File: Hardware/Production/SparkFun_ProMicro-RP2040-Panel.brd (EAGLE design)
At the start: 132.1 x 140 mm, 1611 parts, among them J1 Qwiic, J12 USB Female Type C Connector, J13 Qwiic, J16 USB Female Type C Connector, J17 Qwiic, J2 Qwiic, J20 USB Female Type C Connector, J21 Qwiic, J24 USB Female Type C Connector, J25 Qwiic, J28 USB Female Type C Connector, J29 Qwiic, J32 USB Female Type C Connector, J33 Qwiic, J36 USB Female Type C Connector, J37 Qwiic, J40 USB Female Type C Connector, J41 Qwiic, J44 USB Female Type C Connector, J45 Qwiic, J48 USB Female Type C Connector, J49 Qwiic, J5 USB Female Type C Connector, J52 USB Female Type C Connector, J53 Qwiic, J56 USB Female Type C Connector, J57 Qwiic, J60 USB Female Type C Connector, J8 USB Female Type C Connector, J9 Qwiic, U1 3.3V, U10 RP2040, U11 W25QXX128MBIT, U12 WS2812-2020, U13 3.3V, U14 RP2040, U15 W25QXX128MBIT, U16 WS2812-2020, U17 3.3V, U18 RP2040, U19 W25QXX128MBIT, U2 RP2040, U20 WS2812-2020, U21 3.3V, U22 RP2040, U23 W25QXX128MBIT, U24 WS2812-2020, U25 3.3V, U26 RP2040, U27 W25QXX128MBIT, U28 WS2812-2020, U29 3.3V, U3 WS2812-2020, U30 RP2040, U31 W25QXX128MBIT, U32 WS2812-2020, U33 3.3V, U34 RP2040, U35 W25QXX128MBIT, U36 WS2812-2020, U37 3.3V, U38 RP2040, U39 W25QXX128MBIT, U4 W25QXX128MBIT, U40 WS2812-2020, U41 3.3V, U42 RP2040, U43 W25QXX128MBIT, U44 WS2812-2020, U45 3.3V, U46 RP2040, U47 W25QXX128MBIT, U48 WS2812-2020, U49 3.3V, U5 3.3V, U50 RP2040, U51 W25QXX128MBIT, U52 WS2812-2020, U53 3.3V, U54 RP2040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

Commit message: New panel
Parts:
- added C271, C289, C307, C325, C343, C361, C379, C397, C415: 1.0uF, SparkFun-Capacitors:0402-TIGHT
- added C272, C273, C290, C291, C308, C309, C326, C327, C344, C345, C362, C363, C380, C381, C398, C399, C416, C417: 10uF, SparkFun-Capacitors:0402-TIGHT
- added C274, C275, C292, C293, C310, C311, C328, C329, C346, C347, C364, C365, C382, C383, C400, C401, C418, C419: 15pF, SparkFun-Capacitors:0402-TIGHT
- added C276, C277, C278, C279, C280, C281, C282, C283, C287, C294, C295, C296, C297, C298, C299, C300, C301, C305, C312, C313, C314, C315, C316, C317, C318, C319, C323, C330, C331, C332, C333, C334, C335, C336, C337, C341, C348, C349, C350, C351, C352, C353, C354, C355, C359, C366, C367, C368, C369, C370, C371, C372, C373, C377, C384, C385, C386, C387, C388, C389, C390, C391, C395, C402, C403, C404, C405, C406, C407, C408, C409, C413, C420, C421, C422, C423, C424, C425, C426, C427, C431: 0.1uF, SparkFun-Capacitors:0402-TIGHT
- added C284, C285, C286, C288, C302, C303, C304, C306, C320, C321, C322, C324, C338, C339, C340, C342, C356, C357, C358, C360, C374, C375, C376, C378, C392, C393, C394, C396, C410, C411, C412, C414, C428, C429, C430, C432: 2.2uF, SparkFun-Capacitors:0402-TIGHT
- added D16, D17, D18, D19, D20, D21, D22, D23, D24: 3A/10V/280mV, SparkFun-DiscreteSemi:SOD-323
- added F16, F17, F18, F19, F20, F21, F22, F23, F24: 6V 0.5A, SparkFun-Fuses:0805
- added J61, J65, J69, J73, J77, J81, J85, J89, J93: Qwiic, SparkFun-Connectors:JST04_1MM_RA
- added J62, J63, J66, J67, J70, J71, J74, J75, J78, J79, J82, J83, J86, J87, J90, J91, J94, J95: (no value), Castellated:1X12_CASTELLATED
- added J64, J68, J72, J76, J80, J84, J88, J92, J96: USB Female Type C Connector, SparkFun-Connectors:USB-C-16P_4LAYER-PADS
- added JP46, JP47, JP49, JP50, JP52, JP53, JP55, JP56, JP58, JP59, JP61, JP62, JP64, JP65, JP67, JP68, JP70, JP71: FIDUCIAL1X2, SparkFun-Aesthetics:FIDUCIAL-1X2
- added JP48, JP51, JP54, JP57, JP60, JP63, JP66, JP69, JP72: USB_SOLDER_PADS, SparkFun-Connectors:USB-SOLDER-PADS
- added LED16, LED17, LED18, LED19, LED20, LED21, LED22, LED23, LED24: RED, SparkFun-LED:LED-0603
- added LOGO46, LOGO49, LOGO52, LOGO55, LOGO58, LOGO61, LOGO64, LOGO67, LOGO70: SFE_LOGO_NAME_FLAME.1_INCH, SparkFun-Aesthetics:SFE_LOGO_NAME_FLAME_.1
- added LOGO47, LOGO50, LOGO53, LOGO56, LOGO59, LOGO62, LOGO65, LOGO68, LOGO71: QWIIC_LOGO_6MM, SparkFun-Aesthetics:QWIIC_6MM
- added LOGO48, LOGO51, LOGO54, LOGO57, LOGO60, LOGO63, LOGO66, LOGO69, LOGO72: SFE_LOGO_FLAME.1_INCH, SparkFun-Aesthetics:SFE_LOGO_FLAME_.1
- added R181, R187, R191, R193, R199, R203, R205, R211, R215, R217, R223, R227, R229, R235, R239, R241, R247, R251, R253, R259, R263, R265, R271, R275, R277, R283, R287: 1k, SparkFun-Resistors:0402-TIGHT
- added R182, R192, R194, R204, R206, R216, R218, R228, R230, R240, R242, R252, R254, R264, R266, R276, R278, R288: 10k, SparkFun-Resistors:0402-TIGHT
- added R183, R184, R195, R196, R207, R208, R219, R220, R231, R232, R243, R244, R255, R256, R267, R268, R279, R280: 5.1k, SparkFun-Resistors:0402-TIGHT
- added R185, R186, R197, R198, R209, R210, R221, R222, R233, R234, R245, R246, R257, R258, R269, R270, R281, R282: 2.2k, SparkFun-Resistors:0402-TIGHT
- added R188, R189, R200, R201, R212, R213, R224, R225, R236, R237, R248, R249, R260, R261, R272, R273, R284, R285: 27, SparkFun-Resistors:0402-TIGHT
- added R190, R202, R214, R226, R238, R250, R262, R274, R286: 200, SparkFun-Resistors:0402-TIGHT
- added S31, S33, S35, S37, S39, S41, S43, S45, S47: Reset, SparkFun-Switches:TACTILE_SWITCH_SMD_4.6X2.8MM
- added S32, S34, S36, S38, S40, S42, S44, S46, S48: Boot, SparkFun-Switches:TACTILE_SWITCH_SMD_4.6X2.8MM
- added TP46, TP47, TP48, TP49, TP50, TP51, TP52, TP53, TP54, TP55, TP56, TP57, TP58, TP59, TP60, TP61, TP62, TP63, TP64, TP65, TP66, TP67, TP68, TP69, TP70, TP71, TP72: (no value), SparkFun-Connectors:PAD.03X.05
- added U$1000, U$1030, U$1054, U$1084, U$1108, U$1138, U$1162, U$1192, U$1216, U$1246, U$1270, U$814, U$838, U$868, U$892, U$922, U$946, U$976: (no value), output:A21
- added U$1001, U$1031, U$1055, U$1085, U$1109, U$1139, U$1163, U$1193, U$1217, U$1247, U$1271, U$815, U$839, U$869, U$893, U$923, U$947, U$977: (no value), output:A32
- added U$1002, U$1045, U$1056, U$1099, U$1110, U$1153, U$1164, U$1207, U$1218, U$1261, U$1272, U$829, U$840, U$883, U$894, U$937, U$948, U$991: (no value), output:TX0
- added U$1003, U$1044, U$1057, U$1098, U$1111, U$1152, U$1165, U$1206, U$1219, U$1260, U$1273, U$828, U$841, U$882, U$895, U$936, U$949, U$990: (no value), output:RX1
- added U$1004, U$1017, U$1043, U$1058, U$1071, U$1097, U$1112, U$1125, U$1151, U$1166, U$1179, U$1205, U$1220, U$1233, U$1259, U$1274, U$1287, U$827, U$842, U$855, U$881, U$896, U$909, U$935, U$950, U$963, U$989: (no value), output:GND2
- added U$1005, U$1035, U$1059, U$1089, U$1113, U$1143, U$1167, U$1197, U$1221, U$1251, U$1275, U$819, U$843, U$873, U$897, U$927, U$951, U$981: (no value), output:20
- added U$1006, U$1036, U$1060, U$1090, U$1114, U$1144, U$1168, U$1198, U$1222, U$1252, U$1276, U$820, U$844, U$874, U$898, U$928, U$952, U$982: (no value), output:31
- added U$1007, U$1037, U$1061, U$1091, U$1115, U$1145, U$1169, U$1199, U$1223, U$1253, U$1277, U$821, U$845, U$875, U$899, U$929, U$953, U$983: (no value), output:42
- added U$1008, U$1038, U$1062, U$1092, U$1116, U$1146, U$1170, U$1200, U$1224, U$1254, U$1278, U$822, U$846, U$876, U$900, U$930, U$954, U$984: (no value), output:53
- added U$1009, U$1039, U$1063, U$1093, U$1117, U$1147, U$1171, U$1201, U$1225, U$1255, U$1279, U$823, U$847, U$877, U$901, U$931, U$955, U$985: (no value), output:64
- added U$1010, U$1064, U$1118, U$1172, U$1226, U$1280, U$848, U$902, U$956: (no value), output:D#1
- added U$1011, U$1065, U$1119, U$1173, U$1227, U$1281, U$849, U$903, U$957: (no value), output:D#2
- added U$1012, U$1066, U$1120, U$1174, U$1228, U$1282, U$850, U$904, U$958: (no value), output:G0
- added U$1013, U$1067, U$1121, U$1175, U$1229, U$1283, U$851, U$905, U$959: (no value), output:V3
- added U$1014, U$1068, U$1122, U$1176, U$1230, U$1284, U$852, U$906, U$960: (no value), output:210
- added U$1015, U$1069, U$1123, U$1177, U$1231, U$1285, U$853, U$907, U$961: (no value), output:#RST#0
- added U$1016, U$1070, U$1124, U$1178, U$1232, U$1286, U$854, U$908, U$962: (no value), output:3V3_0
- added U$1018, U$1072, U$1126, U$1180, U$1234, U$1288, U$856, U$910, U$964: (no value), output:RAW0
- added U$1019, U$1073, U$1127, U$1181, U$1235, U$1289, U$857, U$911, U$965: (no value), output:B0
- added U$1020, U$1074, U$1128, U$1182, U$1236, U$1290, U$858, U$912, U$966: (no value), output:R0
- added U$1021, U$1075, U$1129, U$1183, U$1237, U$1291, U$859, U$913, U$967: (no value), output:#0
- added U$1022, U$1076, U$1130, U$1184, U$1238, U$1292, U$860, U$914, U$968: (no value), output:PRO_MICRO0
- added U$1023, U$1077, U$1131, U$1185, U$1239, U$1293, U$861, U$915, U$969: (no value), output:RP20401
- added U$1024, U$1078, U$1132, U$1186, U$1240, U$1294, U$862, U$916, U$970: (no value), output:C0
- added U$1025, U$1079, U$1133, U$1187, U$1241, U$1295, U$863, U$917, U$971: (no value), output:D1
- added U$1026, U$1080, U$1134, U$1188, U$1242, U$1296, U$864, U$918, U$972: (no value), output:DO0
- added U$1027, U$1081, U$1135, U$1189, U$1243, U$811, U$865, U$919, U$973: OSHW-LOGOMINI, SparkFun-Aesthetics:OSHW-LOGO-MINI
- added U$1028, U$1052, U$1082, U$1106, U$1136, U$1160, U$1190, U$1214, U$1244, U$1268, U$812, U$836, U$866, U$890, U$920, U$944, U$974, U$998: (no value), output:A00
- added U$1029, U$1053, U$1083, U$1107, U$1137, U$1161, U$1191, U$1215, U$1245, U$1269, U$813, U$837, U$867, U$891, U$921, U$945, U$975, U$999: (no value), output:A10
- added U$1032, U$1050, U$1086, U$1104, U$1140, U$1158, U$1194, U$1212, U$1248, U$1266, U$816, U$834, U$870, U$888, U$924, U$942, U$978, U$996: (no value), output:CI4
- added U$1033, U$1087, U$1141, U$1195, U$1249, U$817, U$871, U$925, U$979: (no value), output:CO5
- added U$1034, U$1051, U$1088, U$1105, U$1142, U$1159, U$1196, U$1213, U$1250, U$1267, U$818, U$835, U$872, U$889, U$926, U$943, U$980, U$997: (no value), output:SCK3
- added U$1040, U$1094, U$1148, U$1202, U$1256, U$824, U$878, U$932, U$986: (no value), output:#RST#1
- added U$1041, U$1095, U$1149, U$1203, U$1257, U$825, U$879, U$933, U$987: (no value), output:3V30
- added U$1042, U$1096, U$1150, U$1204, U$1258, U$826, U$880, U$934, U$988: (no value), output:PWR0
- added U$1046, U$1100, U$1154, U$1208, U$1262, U$830, U$884, U$938, U$992: (no value), output:GND_0
- added U$1047, U$1101, U$1155, U$1209, U$1263, U$831, U$885, U$939, U$993: (no value), output:70
- added U$1048, U$1102, U$1156, U$1210, U$1264, U$832, U$886, U$940, U$994: (no value), output:81
- added U$1049, U$1103, U$1157, U$1211, U$1265, U$833, U$887, U$941, U$995: (no value), output:92
- added U61, U65, U69, U73, U77, U81, U85, U89, U93: 3.3V, SparkFun-IC-Power:SOT23-5
- added U62, U66, U70, U74, U78, U82, U86, U90, U94: RP2040, RP2040:QFN-56
- added U63, U67, U71, U75, U79, U83, U87, U91, U95: W25QXX128MBIT, SparkFun-IC-Memory:WSON-8-6X5-SKINNY_CENTERPAD
- added U64, U68, U72, U76, U80, U84, U88, U92, U96: WS2812-2020, SparkFun-LED:WS2812-2020
- added Y16, Y17, Y18, Y19, Y20, Y21, Y22, Y23, Y24: 12MHz, SparkFun-Clocks:CRYSTAL-SMD-2X2.5MM
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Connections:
- new net !RESET!15: J63.3, J63.3B, R182.1, S31.3, S31.4, U62.26
- new net !RESET!16: J67.3, J67.3B, R194.1, S33.3, S33.4, U66.26
- new net !RESET!17: J71.3, J71.3B, R206.1, S35.3, S35.4, U70.26
- new net !RESET!18: J75.3, J75.3B, R218.1, S37.3, S37.4, U74.26
- new net !RESET!19: J79.3, J79.3B, R230.1, S39.3, S39.4, U78.26
- new net !RESET!20: J83.3, J83.3B, R242.1, S41.3, S41.4, U82.26
- new net !RESET!21: J87.3, J87.3B, R254.1, S43.3, S43.4, U86.26
- new net !RESET!22: J91.3, J91.3B, R266.1, S45.3, S45.4, U90.26
- new net !RESET!23: J95.3, J95.3B, R278.1, S47.3, S47.4, U94.26
- new net 0/TX15: J62.12, J62.12B, U62.2
- new net 0/TX16: J66.12, J66.12B, U66.2
- new net 0/TX17: J70.12, J70.12B, U70.2
- new net 0/TX18: J74.12, J74.12B, U74.2
- new net 0/TX19: J78.12, J78.12B, U78.2
- new net 0/TX20: J82.12, J82.12B, U82.2
- new net 0/TX21: J86.12, J86.12B, U86.2
- new net 0/TX22: J90.12, J90.12B, U90.2
- new net 0/TX23: J94.12, J94.12B, U94.2
- new net 1.1V15: C282.1, C283.1, C284.1, U62.23, U62.45, U62.50
- new net 1.1V16: C300.1, C301.1, C302.1, U66.23, U66.45, U66.50
- new net 1.1V17: C318.1, C319.1, C320.1, U70.23, U70.45, U70.50
- new net 1.1V18: C336.1, C337.1, C338.1, U74.23, U74.45, U74.50
- new net 1.1V19: C354.1, C355.1, C356.1, U78.23, U78.45, U78.50
- new net 1.1V20: C372.1, C373.1, C374.1, U82.23, U82.45, U82.50
- new net 1.1V21: C390.1, C391.1, C392.1, U86.23, U86.45, U86.50
- new net 1.1V22: C408.1, C409.1, C410.1, U90.23, U90.45, U90.50
- new net 1.1V23: C426.1, C427.1, C428.1, U94.23, U94.45, U94.50
- new net 1/RX15: J62.11, J62.11B, U62.3
- new net 1/RX16: J66.11, J66.11B, U66.3
- new net 1/RX17: J70.11, J70.11B, U70.3
- new net 1/RX18: J74.11, J74.11B, U74.3
- new net 1/RX19: J78.11, J78.11B, U78.3
- new net 1/RX20: J82.11, J82.11B, U82.3
- new net 1/RX21: J86.11, J86.11B, U86.3
- new net 1/RX22: J90.11, J90.11B, U90.3
- new net 1/RX23: J94.11, J94.11B, U94.3
- new net 100: J66.3, J66.3B, U66.9
- new net 101: J66.8, J66.8B, U66.4
- new net 102: J66.7, J66.7B, U66.5
- new net 103: J70.5, J70.5B, U70.7
- new net 104: J70.6, J70.6B, U70.6
- new net 105: J70.4, J70.4B, U70.8
- new net 106: J70.3, J70.3B, U70.9
- new net 107: J70.8, J70.8B, U70.4
- new net 108: J70.7, J70.7B, U70.5
- new net 109: J74.5, J74.5B, U74.7
- new net 110: J74.6, J74.6B, U74.6
- new net 111: J74.4, J74.4B, U74.8
- new net 112: J74.3, J74.3B, U74.9
- new net 113: J74.8, J74.8B, U74.4
- new net 114: J74.7, J74.7B, U74.5
- new net 115: J78.5, J78.5B, U78.7
- new net 116: J78.6, J78.6B, U78.6
- new net 117: J78.4, J78.4B, U78.8
- new net 118: J78.3, J78.3B, U78.9
- new net 119: J78.8, J78.8B, U78.4
- new net 120: J78.7, J78.7B, U78.5
- new net 121: J82.5, J82.5B, U82.7
- new net 122: J82.6, J82.6B, U82.6
- new net 123: J82.4, J82.4B, U82.8
- new net 124: J82.3, J82.3B, U82.9
- new net 125: J82.8, J82.8B, U82.4
- new net 126: J82.7, J82.7B, U82.5
- new net 127: J86.5, J86.5B, U86.7
- new net 128: J86.6, J86.6B, U86.6
- new net 129: J86.4, J86.4B, U86.8
- new net 130: J86.3, J86.3B, U86.9
- new net 131: J86.8, J86.8B, U86.4
- new net 132: J86.7, J86.7B, U86.5
- new net 133: J90.5, J90.5B, U90.7
- new net 134: J90.6, J90.6B, U90.6
- new net 135: J90.4, J90.4B, U90.8
- new net 136: J90.3, J90.3B, U90.9
- new net 137: J90.8, J90.8B, U90.4
- new net 138: J90.7, J90.7B, U90.5
- new net 139: J94.5, J94.5B, U94.7
- new net 140: J94.6, J94.6B, U94.6
- new net 141: J94.4, J94.4B, U94.8
- new net 142: J94.3, J94.3B, U94.9
- new net 143: J94.8, J94.8B, U94.4
- new net 144: J94.7, J94.7B, U94.5
- new net 16/SDA15: J61.3, R185.1, U62.27
- new net 16/SDA16: J65.3, R197.1, U66.27
- new net 16/SDA17: J69.3, R209.1, U70.27
- new net 16/SDA18: J73.3, R221.1, U74.27
- new net 16/SDA19: J77.3, R233.1, U78.27
- new net 16/SDA20: J81.3, R245.1, U82.27
- new net 16/SDA21: J85.3, R257.1, U86.27
- new net 16/SDA22: J89.3, R269.1, U90.27
- new net 16/SDA23: J93.3, R281.1, U94.27
- new net 17/SCL15: J61.4, R186.1, U62.28
- new net 17/SCL16: J65.4, R198.1, U66.28
- new net 17/SCL17: J69.4, R210.1, U70.28
- new net 17/SCL18: J73.4, R222.1, U74.28
- new net 17/SCL19: J77.4, R234.1, U78.28
- new net 17/SCL20: J81.4, R246.1, U82.28
- new net 17/SCL21: J85.4, R258.1, U86.28
- new net 17/SCL22: J89.4, R270.1, U90.28
- new net 17/SCL23: J93.4, R282.1, U94.28
- new net 20/SPI_CIPO15: J63.10, J63.10B, U62.31
- new net 20/SPI_CIPO16: J67.10, J67.10B, U66.31
- new net 20/SPI_CIPO17: J71.10, J71.10B, U70.31
- new net 20/SPI_CIPO18: J75.10, J75.10B, U74.31
- new net 20/SPI_CIPO19: J79.10, J79.10B, U78.31
- new net 20/SPI_CIPO20: J83.10, J83.10B, U82.31
- new net 20/SPI_CIPO21: J87.10, J87.10B, U86.31
- new net 20/SPI_CIPO22: J91.10, J91.10B, U90.31
- new net 20/SPI_CIPO23: J95.10, J95.10B, U94.31
- new net 21/SPI_!CS!15: J63.12, J63.12B, U62.32
- new net 21/SPI_!CS!16: J67.12, J67.12B, U66.32
- new net 21/SPI_!CS!17: J71.12, J71.12B, U70.32
- new net 21/SPI_!CS!18: J75.12, J75.12B, U74.32
- new net 21/SPI_!CS!19: J79.12, J79.12B, U78.32
- new net 21/SPI_!CS!20: J83.12, J83.12B, U82.32
- new net 21/SPI_!CS!21: J87.12, J87.12B, U86.32
- new net 21/SPI_!CS!22: J91.12, J91.12B, U90.32
- new net 21/SPI_!CS!23: J95.12, J95.12B, U94.32
- new net 22/SPI_SCK15: J63.9, J63.9B, U62.34
- new net 22/SPI_SCK16: J67.9, J67.9B, U66.34
- new net 22/SPI_SCK17: J71.9, J71.9B, U70.34
- new net 22/SPI_SCK18: J75.9, J75.9B, U74.34
- new net 22/SPI_SCK19: J79.9, J79.9B, U78.34
- new net 22/SPI_SCK20: J83.9, J83.9B, U82.34
- new net 22/SPI_SCK21: J87.9, J87.9B, U86.34
- new net 22/SPI_SCK22: J91.9, J91.9B, U90.34
- new net 22/SPI_SCK23: J95.9, J95.9B, U94.34
- new net 23/SPI_COPI15: J63.11, J63.11B, U62.35
- new net 23/SPI_COPI16: J67.11, J67.11B, U66.35
- new net 23/SPI_COPI17: J71.11, J71.11B, U70.35
- new net 23/SPI_COPI18: J75.11, J75.11B, U74.35
- new net 23/SPI_COPI19: J79.11, J79.11B, U78.35
- new net 23/SPI_COPI20: J83.11, J83.11B, U82.35
- new net 23/SPI_COPI21: J87.11, J87.11B, U86.35
- new net 23/SPI_COPI22: J91.11, J91.11B, U90.35
- new net 23/SPI_COPI23: J95.11, J95.11B, U94.35
- new net 25/WS2812-DI15: U62.37, U64.3
- new net 25/WS2812-DI16: U66.37, U68.3
- new net 25/WS2812-DI17: U70.37, U72.3
- new net 25/WS2812-DI18: U74.37, U76.3
- new net 25/WS2812-DI19: U78.37, U80.3
- new net 25/WS2812-DI20: U82.37, U84.3
- new net 25/WS2812-DI21: U86.37, U88.3
- new net 25/WS2812-DI22: U90.37, U92.3
- new net 25/WS2812-DI23: U94.37, U96.3
- new net 3.3V15: C273.2, C276.1, C277.1, C278.1, C279.1, C280.1, C281.1, C285.1, C287.1, C288.1, J61.2, J63.4, J63.4B, R181.2, R182.2, R185.2, R186.2, R190.2, R192.2, U61.5, U62.1, U62.10, U62.22, U62.33, U62.42, U62.44, U62.48, U62.49, U63.8
- new net 3.3V16: C291.2, C294.1, C295.1, C296.1, C297.1, C298.1, C299.1, C303.1, C305.1, C306.1, J65.2, J67.4, J67.4B, R193.2, R194.2, R197.2, R198.2, R202.2, R204.2, U65.5, U66.1, U66.10, U66.22, U66.33, U66.42, U66.44, U66.48, U66.49, U67.8
- new net 3.3V17: C309.2, C312.1, C313.1, C314.1, C315.1, C316.1, C317.1, C321.1, C323.1, C324.1, J69.2, J71.4, J71.4B, R205.2, R206.2, R209.2, R210.2, R214.2, R216.2, U69.5, U70.1, U70.10, U70.22, U70.33, U70.42, U70.44, U70.48, U70.49, U71.8
- new net 3.3V18: C327.2, C330.1, C331.1, C332.1, C333.1, C334.1, C335.1, C339.1, C341.1, C342.1, J73.2, J75.4, J75.4B, R217.2, R218.2, R221.2, R222.2, R226.2, R228.2, U73.5, U74.1, U74.10, U74.22, U74.33, U74.42, U74.44, U74.48, U74.49, U75.8
- new net 3.3V19: C345.2, C348.1, C349.1, C350.1, C351.1, C352.1, C353.1, C357.1, C359.1, C360.1, J77.2, J79.4, J79.4B, R229.2, R230.2, R233.2, R234.2, R238.2, R240.2, U77.5, U78.1, U78.10, U78.22, U78.33, U78.42, U78.44, U78.48, U78.49, U79.8
- new net 3.3V20: C363.2, C366.1, C367.1, C368.1, C369.1, C370.1, C371.1, C375.1, C377.1, C378.1, J81.2, J83.4, J83.4B, R241.2, R242.2, R245.2, R246.2, R250.2, R252.2, U81.5, U82.1, U82.10, U82.22, U82.33, U82.42, U82.44, U82.48, U82.49, U83.8
- new net 3.3V21: C381.2, C384.1, C385.1, C386.1, C387.1, C388.1, C389.1, C393.1, C395.1, C396.1, J85.2, J87.4, J87.4B, R253.2, R254.2, R257.2, R258.2, R262.2, R264.2, U85.5, U86.1, U86.10, U86.22, U86.33, U86.42, U86.44, U86.48, U86.49, U87.8
- new net 3.3V22: C399.2, C402.1, C403.1, C404.1, C405.1, C406.1, C407.1, C411.1, C413.1, C414.1, J89.2, J91.4, J91.4B, R265.2, R266.2, R269.2, R270.2, R274.2, R276.2, U89.5, U90.1, U90.10, U90.22, U90.33, U90.42, U90.44, U90.48, U90.49, U91.8
- new net 3.3V23: C417.2, C420.1, C421.1, C422.1, C423.1, C424.1, C425.1, C429.1, C431.1, C432.1, J93.2, J95.4, J95.4B, R277.2, R278.2, R281.2, R282.2, R286.2, R288.2, U93.5, U94.1, U94.10, U94.22, U94.33, U94.42, U94.44, U94.48, U94.49, U95.8
- new net 8/TX16: J62.2, J62.2B, U62.11
- new net 8/TX17: J66.2, J66.2B, U66.11
- new net 8/TX18: J70.2, J70.2B, U70.11
- new net 8/TX19: J74.2, J74.2B, U74.11
- new net 8/TX20: J78.2, J78.2B, U78.11
- new net 8/TX21: J82.2, J82.2B, U82.11
- new net 8/TX22: J86.2, J86.2B, U86.11
- new net 8/TX23: J90.2, J90.2B, U90.11
- new net 8/TX24: J94.2, J94.2B, U94.11
- new net 9/RX16: J62.1, J62.1B, U62.12
- new net 9/RX17: J66.1, J66.1B, U66.12
- new net 9/RX18: J70.1, J70.1B, U70.12
- new net 9/RX19: J74.1, J74.1B, U74.12
- new net 9/RX20: J78.1, J78.1B, U78.12
- new net 9/RX21: J82.1, J82.1B, U82.12
- new net 9/RX22: J86.1, J86.1B, U86.12
- new net 9/RX23: J90.1, J90.1B, U90.12
- new net 9/RX24: J94.1, J94.1B, U94.12
- new net 91: J62.5, J62.5B, U62.7
- new net 92: J62.6, J62.6B, U62.6
- new net 93: J62.4, J62.4B, U62.8
- new net 94: J62.3, J62.3B, U62.9
- new net 95: J62.8, J62.8B, U62.4
- new net 96: J62.7, J62.7B, U62.5
- new net 97: J66.5, J66.5B, U66.7
- new net 98: J66.6, J66.6B, U66.6
- new net 99: J66.4, J66.4B, U66.8
- new net A60: J63.5, J63.5B, U62.41
- new net A61: J63.6, J63.6B, U62.40
- new net A62: J63.7, J63.7B, U62.39
- new net A63: J63.8, J63.8B, U62.38
- new net A64: J67.5, J67.5B, U66.41
- new net A65: J67.6, J67.6B, U66.40
- new net A66: J67.7, J67.7B, U66.39
- new net A67: J67.8, J67.8B, U66.38
- new net A68: J71.5, J71.5B, U70.41
- new net A69: J71.6, J71.6B, U70.40
- new net A70: J71.7, J71.7B, U70.39
- new net A71: J71.8, J71.8B, U70.38
- new net A72: J75.5, J75.5B, U74.41
- new net A73: J75.6, J75.6B, U74.40
- new net A74: J75.7, J75.7B, U74.39
- new net A75: J75.8, J75.8B, U74.38
- new net A76: J79.5, J79.5B, U78.41
- new net A77: J79.6, J79.6B, U78.40
- new net A78: J79.7, J79.7B, U78.39
- new net A79: J79.8, J79.8B, U78.38
- new net A80: J83.5, J83.5B, U82.41
- new net A81: J83.6, J83.6B, U82.40
- new net A82: J83.7, J83.7B, U82.39
- new net A83: J83.8, J83.8B, U82.38
- new net A84: J87.5, J87.5B, U86.41
- new net A85: J87.6, J87.6B, U86.40
- new net A86: J87.7, J87.7B, U86.39
- new net A87: J87.8, J87.8B, U86.38
- new net A88: J91.5, J91.5B, U90.41
- new net A89: J91.6, J91.6B, U90.40
- new net A90: J91.7, J91.7B, U90.39
- new net A91: J91.8, J91.8B, U90.38
- new net A92: J95.5, J95.5B, U94.41
- new net A93: J95.6, J95.6B, U94.40
- new net A94: J95.7, J95.7B, U94.39
- new net A95: J95.8, J95.8B, U94.38
- new net ADC_VDD15: C286.1, R190.1, U62.43
- new net ADC_VDD16: C304.1, R202.1, U66.43
- new net ADC_VDD17: C322.1, R214.1, U70.43
- new net ADC_VDD18: C340.1, R226.1, U74.43
- new net ADC_VDD19: C358.1, R238.1, U78.43
- new net ADC_VDD20: C376.1, R250.1, U82.43
- new net ADC_VDD21: C394.1, R262.1, U86.43
- new net ADC_VDD22: C412.1, R274.1, U90.43
- new net ADC_VDD23: C430.1, R286.1, U94.43
- new net BOOT15: R191.2, S32.3, S32.4
- new net BOOT16: R203.2, S34.3, S34.4
- new net BOOT17: R215.2, S36.3, S36.4
- new net BOOT18: R227.2, S38.3, S38.4
- new net BOOT19: R239.2, S40.3, S40.4
- new net BOOT20: R251.2, S42.3, S42.4
- new net BOOT21: R263.2, S44.3, S44.4
- new net BOOT22: R275.2, S46.3, S46.4
- new net BOOT23: R287.2, S48.3, S48.4
- new net GND15: C271.1, C272.1, C273.1, C274.1, C275.1, C276.2, C277.2, C278.2, C279.2, C280.2, C281.2, C282.2, C283.2, C284.2, C285.2, C286.2, C287.2, C288.2, J61.1, J62.10, J62.10B, J62.9, J62.9B, J63.2, J63.2B, J64.GND, J64.GND2, JP48.GND, LED16.C, R183.1, R184.1, S31.1, S31.2, S32.1, S32.2, U61.2, U62.19, U62.EPAD, U63.4, U64.2
- new net GND16: C289.1, C290.1, C291.1, C292.1, C293.1, C294.2, C295.2, C296.2, C297.2, C298.2, C299.2, C300.2, C301.2, C302.2, C303.2, C304.2, C305.2, C306.2, J65.1, J66.10, J66.10B, J66.9, J66.9B, J67.2, J67.2B, J68.GND, J68.GND2, JP51.GND, LED17.C, R195.1, R196.1, S33.1, S33.2, S34.1, S34.2, U65.2, U66.19, U66.EPAD, U67.4, U68.2
- new net GND17: C307.1, C308.1, C309.1, C310.1, C311.1, C312.2, C313.2, C314.2, C315.2, C316.2, C317.2, C318.2, C319.2, C320.2, C321.2, C322.2, C323.2, C324.2, J69.1, J70.10, J70.10B, J70.9, J70.9B, J71.2, J71.2B, J72.GND, J72.GND2, JP54.GND, LED18.C, R207.1, R208.1, S35.1, S35.2, S36.1, S36.2, U69.2, U70.19, U70.EPAD, U71.4, U72.2
- new net GND18: C325.1, C326.1, C327.1, C328.1, C329.1, C330.2, C331.2, C332.2, C333.2, C334.2, C335.2, C336.2, C337.2, C338.2, C339.2, C340.2, C341.2, C342.2, J73.1, J74.10, J74.10B, J74.9, J74.9B, J75.2, J75.2B, J76.GND, J76.GND2, JP57.GND, LED19.C, R219.1, R220.1, S37.1, S37.2, S38.1, S38.2, U73.2, U74.19, U74.EPAD, U75.4, U76.2
- new net GND19: C343.1, C344.1, C345.1, C346.1, C347.1, C348.2, C349.2, C350.2, C351.2, C352.2, C353.2, C354.2, C355.2, C356.2, C357.2, C358.2, C359.2, C360.2, J77.1, J78.10, J78.10B, J78.9, J78.9B, J79.2, J79.2B, J80.GND, J80.GND2, JP60.GND, LED20.C, R231.1, R232.1, S39.1, S39.2, S40.1, S40.2, U77.2, U78.19, U78.EPAD, U79.4, U80.2
- new net GND20: C361.1, C362.1, C363.1, C364.1, C365.1, C366.2, C367.2, C368.2, C369.2, C370.2, C371.2, C372.2, C373.2, C374.2, C375.2, C376.2, C377.2, C378.2, J81.1, J82.10, J82.10B, J82.9, J82.9B, J83.2, J83.2B, J84.GND, J84.GND2, JP63.GND, LED21.C, R243.1, R244.1, S41.1, S41.2, S42.1, S42.2, U81.2, U82.19, U82.EPAD, U83.4, U84.2
- new net GND21: C379.1, C380.1, C381.1, C382.1, C383.1, C384.2, C385.2, C386.2, C387.2, C388.2, C389.2, C390.2, C391.2, C392.2, C393.2, C394.2, C395.2, C396.2, J85.1, J86.10, J86.10B, J86.9, J86.9B, J87.2, J87.2B, J88.GND, J88.GND2, JP66.GND, LED22.C, R255.1, R256.1, S43.1, S43.2, S44.1, S44.2, U85.2, U86.19, U86.EPAD, U87.4, U88.2
- new net GND22: C397.1, C398.1, C399.1, C400.1, C401.1, C402.2, C403.2, C404.2, C405.2, C406.2, C407.2, C408.2, C409.2, C410.2, C411.2, C412.2, C413.2, C414.2, J89.1, J90.10, J90.10B, J90.9, J90.9B, J91.2, J91.2B, J92.GND, J92.GND2, JP69.GND, LED23.C, R267.1, R268.1, S45.1, S45.2, S46.1, S46.2, U89.2, U90.19, U90.EPAD, U91.4, U92.2
- new net GND23: C415.1, C416.1, C417.1, C418.1, C419.1, C420.2, C421.2, C422.2, C423.2, C424.2, C425.2, C426.2, C427.2, C428.2, C429.2, C430.2, C431.2, C432.2, J93.1, J94.10, J94.10B, J94.9, J94.9B, J95.2, J95.2B, J96.GND, J96.GND2, JP72.GND, LED24.C, R279.1, R280.1, S47.1, S47.2, S48.1, S48.2, U93.2, U94.19, U94.EPAD, U95.4, U96.2
- new net N$61: LED16.A, R181.1
- new net N$62: J64.A5, R184.2
- new net N$63: J64.B5, R183.2
- new net N$64: TP48.P$1, U64.1
- new net N$65: LED17.A, R193.1
- new net N$66: J68.A5, R196.2
- new net N$67: J68.B5, R195.2
- new net N$68: TP51.P$1, U68.1
- new net N$69: LED18.A, R205.1
- new net N$70: J72.A5, R208.2
- new net N$71: J72.B5, R207.2
- new net N$72: TP54.P$1, U72.1
- new net N$73: LED19.A, R217.1
- new net N$74: J76.A5, R220.2
- new net N$75: J76.B5, R219.2
- new net N$76: TP57.P$1, U76.1
- new net N$77: LED20.A, R229.1
- new net N$78: J80.A5, R232.2
- new net N$79: J80.B5, R231.2
- new net N$80: TP60.P$1, U80.1
- new net N$81: LED21.A, R241.1
- new net N$82: J84.A5, R244.2
- new net N$83: J84.B5, R243.2
- new net N$84: TP63.P$1, U84.1
- new net N$85: LED22.A, R253.1
- new net N$86: J88.A5, R256.2
- new net N$87: J88.B5, R255.2
- new net N$88: TP66.P$1, U88.1
- new net N$89: LED23.A, R265.1
- new net N$90: J92.A5, R268.2
- new net N$91: J92.B5, R267.2
- new net N$92: TP69.P$1, U92.1
- new net N$93: LED24.A, R277.1
- new net N$94: J96.A5, R280.2
- new net N$95: J96.B5, R279.2
- new net N$96: TP72.P$1, U96.1
- new net QSPI-60: U62.53, U63.5
- new net QSPI-61: U62.51, U63.7
- new net QSPI-62: U62.55, U63.2
- new net QSPI-63: U62.54, U63.3
- new net QSPI-64: U66.53, U67.5
- new net QSPI-65: U66.51, U67.7
- new net QSPI-66: U66.55, U67.2
- new net QSPI-67: U66.54, U67.3
- new net QSPI-68: U70.53, U71.5
- new net QSPI-69: U70.51, U71.7
- new net QSPI-70: U70.55, U71.2
- new net QSPI-71: U70.54, U71.3
- new net QSPI-72: U74.53, U75.5
- new net QSPI-73: U74.51, U75.7
- new net QSPI-74: U74.55, U75.2
- new net QSPI-75: U74.54, U75.3
- new net QSPI-76: U78.53, U79.5
- new net QSPI-77: U78.51, U79.7
- new net QSPI-78: U78.55, U79.2
- new net QSPI-79: U78.54, U79.3
- new net QSPI-80: U82.53, U83.5
- new net QSPI-81: U82.51, U83.7
- new net QSPI-82: U82.55, U83.2
- new net QSPI-83: U82.54, U83.3
- new net QSPI-84: U86.53, U87.5
- new net QSPI-85: U86.51, U87.7
- new net QSPI-86: U86.55, U87.2
- new net QSPI-87: U86.54, U87.3
- new net QSPI-88: U90.53, U91.5
- new net QSPI-89: U90.51, U91.7
- new net QSPI-90: U90.55, U91.2
- new net QSPI-91: U90.54, U91.3
- new net QSPI-92: U94.53, U95.5
- new net QSPI-93: U94.51, U95.7
- new net QSPI-94: U94.55, U95.2
- new net QSPI-95: U94.54, U95.3
- new net QSPI-CLK15: U62.52, U63.6
- new net QSPI-CLK16: U66.52, U67.6
- new net QSPI-CLK17: U70.52, U71.6
- new net QSPI-CLK18: U74.52, U75.6
- new net QSPI-CLK19: U78.52, U79.6
- new net QSPI-CLK20: U82.52, U83.6
- new net QSPI-CLK21: U86.52, U87.6
- new net QSPI-CLK22: U90.52, U91.6
- new net QSPI-CLK23: U94.52, U95.6
- new net QSPI-CS15: R191.1, R192.1, U62.56, U63.1
- new net QSPI-CS16: R203.1, R204.1, U66.56, U67.1
- new net QSPI-CS17: R215.1, R216.1, U70.56, U71.1
- new net QSPI-CS18: R227.1, R228.1, U74.56, U75.1
- new net QSPI-CS19: R239.1, R240.1, U78.56, U79.1
- new net QSPI-CS20: R251.1, R252.1, U82.56, U83.1
- new net QSPI-CS21: R263.1, R264.1, U86.56, U87.1
- new net QSPI-CS22: R275.1, R276.1, U90.56, U91.1
- new net QSPI-CS23: R287.1, R288.1, U94.56, U95.1
- new net RAW15: C272.2, D16.C, J63.1, J63.1B, U61.1, U61.3, U64.4
- new net RAW16: C290.2, D17.C, J67.1, J67.1B, U65.1, U65.3, U68.4
- new net RAW17: C308.2, D18.C, J71.1, J71.1B, U69.1, U69.3, U72.4
- new net RAW18: C326.2, D19.C, J75.1, J75.1B, U73.1, U73.3, U76.4
- new net RAW19: C344.2, D20.C, J79.1, J79.1B, U77.1, U77.3, U80.4
- new net RAW20: C362.2, D21.C, J83.1, J83.1B, U81.1, U81.3, U84.4
- new net RAW21: C380.2, D22.C, J87.1, J87.1B, U85.1, U85.3, U88.4
- new net RAW22: C398.2, D23.C, J91.1, J91.1B, U89.1, U89.3, U92.4
- new net RAW23: C416.2, D24.C, J95.1, J95.1B, U93.1, U93.3, U96.4
- new net RP_D+15: J64.A6, J64.B6, JP48.D+, R189.1
- new net RP_D+16: J68.A6, J68.B6, JP51.D+, R201.1
- new net RP_D+17: J72.A6, J72.B6, JP54.D+, R213.1
- new net RP_D+18: J76.A6, J76.B6, JP57.D+, R225.1
- new net RP_D+19: J80.A6, J80.B6, JP60.D+, R237.1
- new net RP_D+20: J84.A6, J84.B6, JP63.D+, R249.1
- new net RP_D+21: J88.A6, J88.B6, JP66.D+, R261.1
- new net RP_D+22: J92.A6, J92.B6, JP69.D+, R273.1
- new net RP_D+23: J96.A6, J96.B6, JP72.D+, R285.1
- new net RP_D-15: J64.A7, J64.B7, JP48.D-, R188.1
- new net RP_D-16: J68.A7, J68.B7, JP51.D-, R200.1
- new net RP_D-17: J72.A7, J72.B7, JP54.D-, R212.1
- new net RP_D-18: J76.A7, J76.B7, JP57.D-, R224.1
- new net RP_D-19: J80.A7, J80.B7, JP60.D-, R236.1
- new net RP_D-20: J84.A7, J84.B7, JP63.D-, R248.1
- new net RP_D-21: J88.A7, J88.B7, JP66.D-, R260.1
- new net RP_D-22: J92.A7, J92.B7, JP69.D-, R272.1
- new net RP_D-23: J96.A7, J96.B7, JP72.D-, R284.1
- new net RP_D1+15: R189.2, U62.47
- new net RP_D1+16: R201.2, U66.47
- new net RP_D1+17: R213.2, U70.47
- new net RP_D1+18: R225.2, U74.47
- new net RP_D1+19: R237.2, U78.47
- new net RP_D1+20: R249.2, U82.47
- new net RP_D1+21: R261.2, U86.47
- new net RP_D1+22: R273.2, U90.47
- new net RP_D1+23: R285.2, U94.47
- new net RP_D1-15: R188.2, U62.46
- new net RP_D1-16: R200.2, U66.46
- new net RP_D1-17: R212.2, U70.46
- new net RP_D1-18: R224.2, U74.46
- new net RP_D1-19: R236.2, U78.46
- new net RP_D1-20: R248.2, U82.46
- new net RP_D1-21: R260.2, U86.46
- new net RP_D1-22: R272.2, U90.46
- new net RP_D1-23: R284.2, U94.46
- new net SWDCK15: TP46.P$1, U62.24
- new net SWDCK16: TP49.P$1, U66.24
- new net SWDCK17: TP52.P$1, U70.24
- new net SWDCK18: TP55.P$1, U74.24
- new net SWDCK19: TP58.P$1, U78.24
- new net SWDCK20: TP61.P$1, U82.24
- new net SWDCK21: TP64.P$1, U86.24
- new net SWDCK22: TP67.P$1, U90.24
- new net SWDCK23: TP70.P$1, U94.24
- new net SWDIO15: TP47.P$1, U62.25
- new net SWDIO16: TP50.P$1, U66.25
- new net SWDIO17: TP53.P$1, U70.25
- new net SWDIO18: TP56.P$1, U74.25
- new net SWDIO19: TP59.P$1, U78.25
- new net SWDIO20: TP62.P$1, U82.25
- new net SWDIO21: TP65.P$1, U86.25
- new net SWDIO22: TP68.P$1, U90.25
- new net SWDIO23: TP71.P$1, U94.25
- new net USB_RAW15: D16.A, F16.2
- new net USB_RAW16: D17.A, F17.2
- new net USB_RAW17: D18.A, F18.2
- new net USB_RAW18: D19.A, F19.2
- new net USB_RAW19: D20.A, F20.2
- new net USB_RAW20: D21.A, F21.2
- new net USB_RAW21: D22.A, F22.2
- new net USB_RAW22: D23.A, F23.2
- new net USB_RAW23: D24.A, F24.2
- new net V_USB15: C271.2, F16.1, J64.VBUS1, J64.VBUS2, JP48.VBUS
- new net V_USB16: C289.2, F17.1, J68.VBUS1, J68.VBUS2, JP51.VBUS
- new net V_USB17: C307.2, F18.1, J72.VBUS1, J72.VBUS2, JP54.VBUS
- new net V_USB18: C325.2, F19.1, J76.VBUS1, J76.VBUS2, JP57.VBUS
- new net V_USB19: C343.2, F20.1, J80.VBUS1, J80.VBUS2, JP60.VBUS
- new net V_USB20: C361.2, F21.1, J84.VBUS1, J84.VBUS2, JP63.VBUS
- new net V_USB21: C379.2, F22.1, J88.VBUS1, J88.VBUS2, JP66.VBUS
- new net V_USB22: C397.2, F23.1, J92.VBUS1, J92.VBUS2, JP69.VBUS
- new net V_USB23: C415.2, F24.1, J96.VBUS1, J96.VBUS2, JP72.VBUS
- new net X16: C275.2, U62.20, Y16.P3
- new net X17: C293.2, U66.20, Y17.P3
- new net X18: C311.2, U70.20, Y18.P3
- new net X19: C329.2, U74.20, Y19.P3
- new net X1A15: R187.2, U62.21
- new net X1A16: R199.2, U66.21
- new net X1A17: R211.2, U70.21
- new net X1A18: R223.2, U74.21
- new net X1A19: R235.2, U78.21
- new net X1A20: R247.2, U82.21
- new net X1A21: R259.2, U86.21
- new net X1A22: R271.2, U90.21
- new net X1A23: R283.2, U94.21
- new net X1B15: C274.2, R187.1, Y16.P1
- new net X1B16: C292.2, R199.1, Y17.P1
- new net X1B17: C310.2, R211.1, Y18.P1
- new net X1B18: C328.2, R223.1, Y19.P1
- new net X1B19: C346.2, R235.1, Y20.P1
- new net X1B20: C364.2, R247.1, Y21.P1
- new net X1B21: C382.2, R259.1, Y22.P1
- new net X1B22: C400.2, R271.1, Y23.P1
- new net X1B23: C418.2, R283.1, Y24.P1
- new net X20: C347.2, U78.20, Y20.P3
- new net X21: C365.2, U82.20, Y21.P3
- new net X22: C383.2, U86.20, Y22.P3
- new net X23: C401.2, U90.20, Y23.P3
- new net X24: C419.2, U94.20, Y24.P3
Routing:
- net 3.3V20: track 0.00 -> 43.5 mm, vias 0 -> 10
- net 3.3V22: track 0.00 -> 43.5 mm, vias 0 -> 10
- net 3.3V21: track 0.00 -> 43.5 mm, vias 0 -> 10
- net 3.3V19: track 0.00 -> 43.5 mm, vias 0 -> 10
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- added copper zone on layer 15, net 3.3V15
- added copper zone on layer 15, net 3.3V16
- added copper zone on layer 15, net 3.3V17
- added copper zone on layer 15, net 3.3V18
- added copper zone on layer 15, net 3.3V19
- added copper zone on layer 15, net 3.3V20
- added copper zone on layer 15, net 3.3V21
- added copper zone on layer 15, net 3.3V22
- added copper zone on layer 15, net 3.3V23
- added copper zone on layer 1, net GND15
- added copper zone on layer 16, net GND15
- added copper zone on layer 2, net GND15
- added copper zone on layer 1, net GND16
- added copper zone on layer 16, net GND16
- added copper zone on layer 2, net GND16
- added copper zone on layer 1, net GND17
- added copper zone on layer 16, net GND17
- added copper zone on layer 2, net GND17
- added copper zone on layer 1, net GND18
- added copper zone on layer 16, net GND18
- added copper zone on layer 2, net GND18
- added copper zone on layer 1, net GND19
- added copper zone on layer 16, net GND19
- added copper zone on layer 2, net GND19
- added copper zone on layer 1, net GND20
- added copper zone on layer 16, net GND20
- added copper zone on layer 2, net GND20
- added copper zone on layer 1, net GND21
- added copper zone on layer 16, net GND21
- added copper zone on layer 2, net GND21
- added copper zone on layer 1, net GND22
- added copper zone on layer 16, net GND22
- added copper zone on layer 2, net GND22
- added copper zone on layer 1, net GND23
- added copper zone on layer 16, net GND23
- added copper zone on layer 2, net GND23
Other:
- board size 132.1 x 140 mm -> 212.1 x 134.6 mm
- board text added: "v-score"
- board text added: "v12"
- board text removed: "v11"

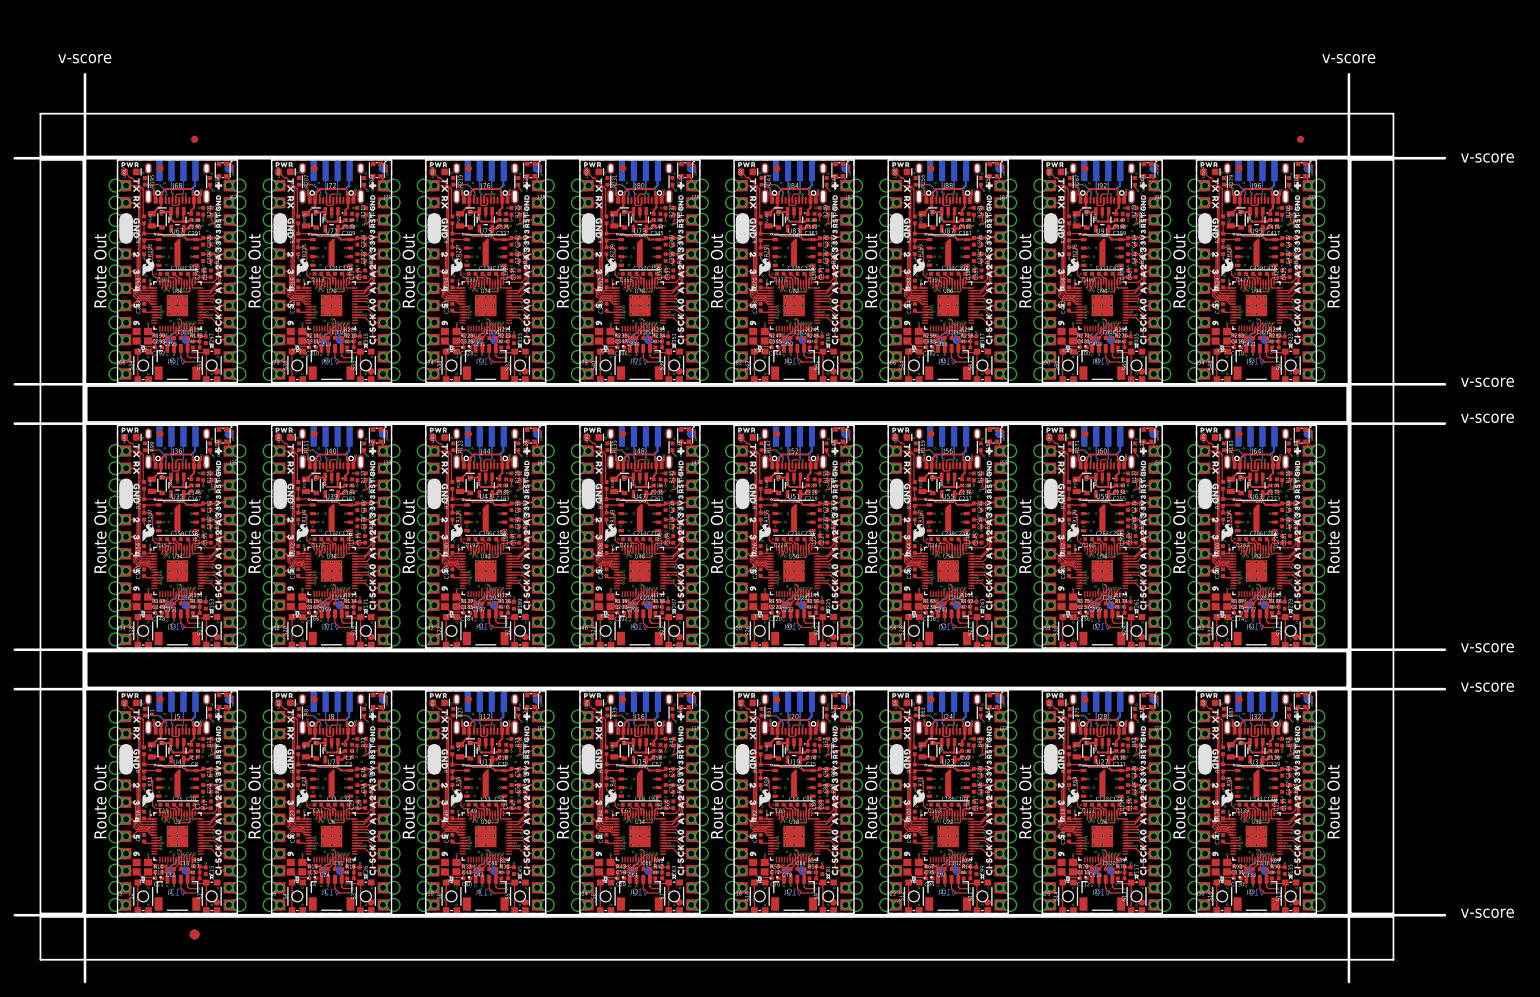
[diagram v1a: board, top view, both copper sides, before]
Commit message: Increase isolation in layers 2/15. Increase to v13.
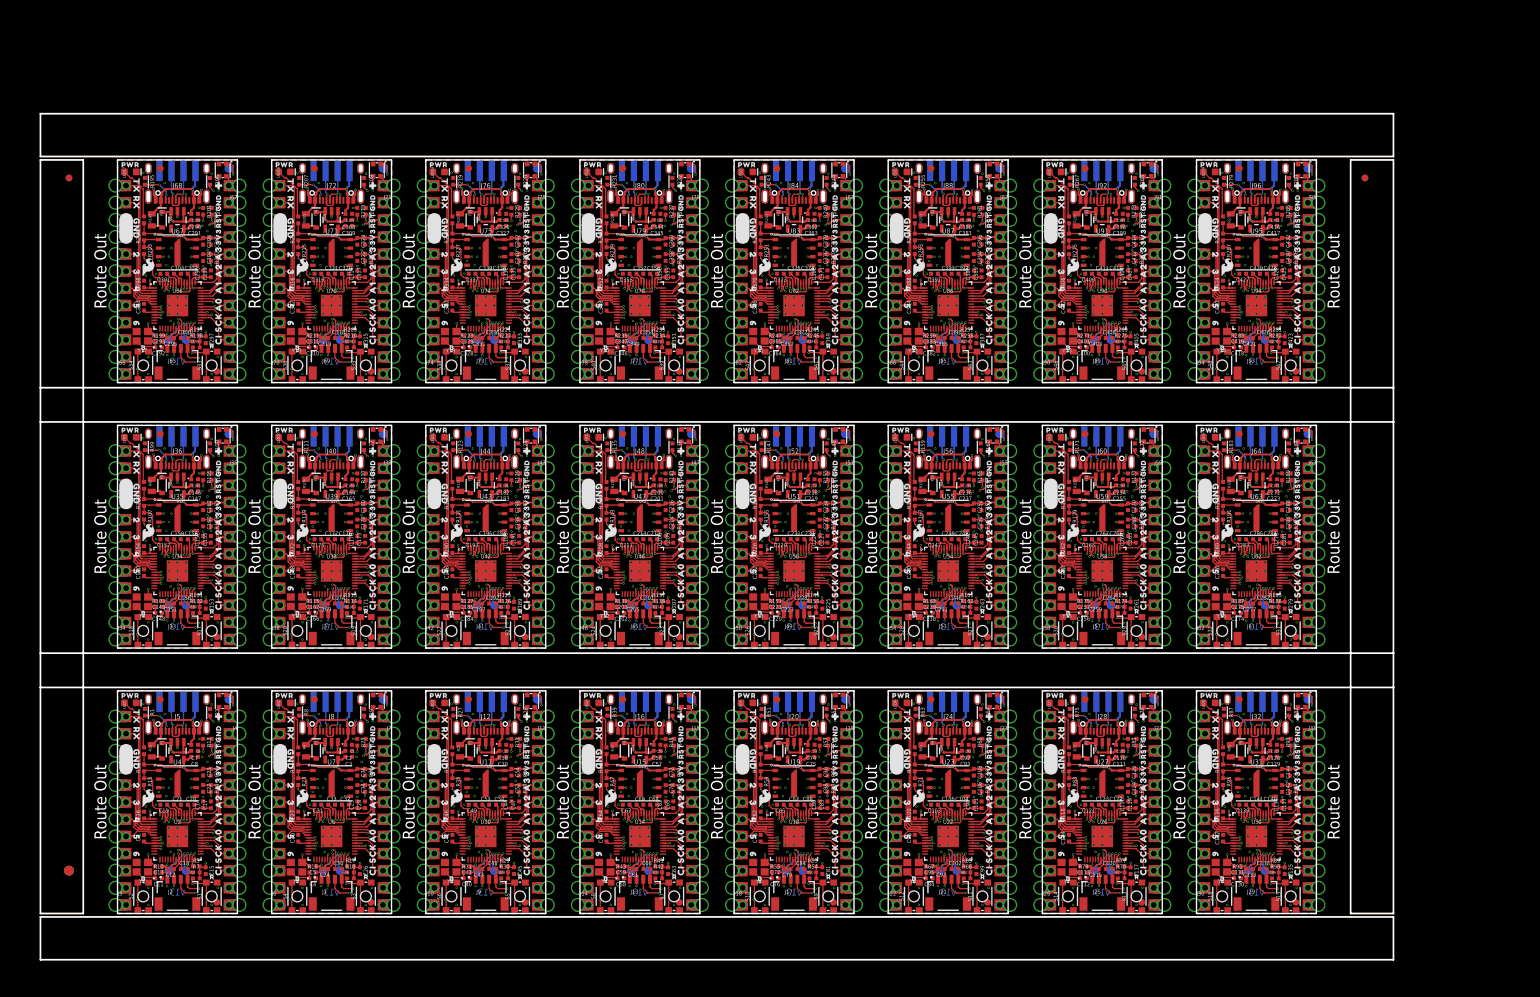
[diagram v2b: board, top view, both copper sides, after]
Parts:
- moved E$5 20.9 mm to (-7.20, 6.35)
- moved E$6 20.9 mm to (-7.20, 6.35)
- moved E$1 19.5 mm to (-7.20, 109.1)
- moved E$2 19.5 mm to (-7.20, 109.1)
- moved E$3 11.1 mm to (185.0, 109.1)
- moved E$4 11.1 mm to (185.0, 109.1)
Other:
- board size 212.1 x 134.6 mm -> 200.7 x 125.5 mm
- board text added: "v13"
- board text removed: "v-score"
- board text removed: "v12"
